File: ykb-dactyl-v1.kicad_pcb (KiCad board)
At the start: 2 copper layers, 1 part

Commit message: Update
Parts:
- removed U1: ~, holyiot-21069:holyiot-21069
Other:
- board outline added: 55.8 x 58.3 mm

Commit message: Update
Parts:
- added C1: C, Capacitor_SMD:C_0402_1005Metric, F.Cu at (128.1, 152.2)
- added C60: 0.1uF, Capacitor_SMD:C_0402_1005Metric, F.Cu at (130.9, 135.5)
- added C61: 0.1uF, Capacitor_SMD:C_0402_1005Metric, F.Cu at (130.9, 137.4)
- added IC1: TXU0101DCKR, footprints:SOT65P210X110-6N, F.Cu at (131.8, 132.6)
- added J1: JST_SH_BM10B-SRSS-TB_1x10-1MP_P1.00mm_Vertical, Connector_JST:JST_SH_BM10B-SRSS-TB_1x10-1MP_P1.00mm_Vertical, F.Cu at (90.0, 52.5)
- added J2: JST_SH_BM10B-SRSS-TB_1x10-1MP_P1.00mm_Vertical, Connector_JST:JST_SH_BM10B-SRSS-TB_1x10-1MP_P1.00mm_Vertical, F.Cu at (90.0, 58.0)
- added J3: JST_SH_BM10B-SRSS-TB_1x10-1MP_P1.00mm_Vertical, Connector_JST:JST_SH_BM10B-SRSS-TB_1x10-1MP_P1.00mm_Vertical, F.Cu at (90.0, 63.5)
- added J4: JST_SH_BM10B-SRSS-TB_1x10-1MP_P1.00mm_Vertical, Connector_JST:JST_SH_BM10B-SRSS-TB_1x10-1MP_P1.00mm_Vertical, F.Cu at (90.0, 69.0)
- added J5: JST_SH_BM10B-SRSS-TB_1x10-1MP_P1.00mm_Vertical, Connector_JST:JST_SH_BM10B-SRSS-TB_1x10-1MP_P1.00mm_Vertical, F.Cu at (87.8, 149.4)
- added J6: JST_SH_BM10B-SRSS-TB_1x10-1MP_P1.00mm_Vertical, Connector_JST:JST_SH_BM10B-SRSS-TB_1x10-1MP_P1.00mm_Vertical, F.Cu at (87.8, 155.6)
- added J7: JST_SH_BM12B-SRSS-TB_1x12-1MP_P1.00mm_Vertical, Connector_JST:JST_SH_BM12B-SRSS-TB_1x12-1MP_P1.00mm_Vertical, F.Cu at (103.6, 149.6)
- added J8: MC-121-L124, MC-121-L124:MC-121-L124, F.Cu at (90.1, 39.8)
- added J9: Conn_ARM_SWD_TagConnect_TC2030, Connector:Tag-Connect_TC2030-IDC-FP_2x03_P1.27mm_Vertical, F.Cu at (134.2, 126.0)
- added R1: 100K, Resistor_SMD:R_0402_1005Metric, F.Cu at (132.5, 152.0)
- added S1: DG9408EDN-T1-GE4, footprints:QFN65P400X400X95-17N-D, F.Cu at (98.4, 124.4)
- added S2: DG9408EDN-T1-GE4, footprints:QFN65P400X400X95-17N-D, F.Cu at (98.4, 130.7)
- added S3: DG9408EDN-T1-GE4, footprints:QFN65P400X400X95-17N-D, F.Cu at (98.4, 137.0)
- added S4: DG9408EDN-T1-GE4, footprints:QFN65P400X400X95-17N-D, F.Cu at (98.4, 143.3)
- added U1: holyiot-21069, holyiot-21069:holyiot-21069, F.Cu at (97.2, 78.2)
- added U2: XC6193A103ER-G, footprints:SON40P150X150X50-9N, F.Cu at (133.3, 149.4)
- added U3: TPS631000DRLR, footprints:SOT50P160X60-8N, F.Cu at (133.5, 145.6)
- added U4: TPS62840DLCR, footprints:SON50P200X150X100-8N, F.Cu at (129.2, 149.5)
- added U5: BQ25185DLHR, footprints:SON40P220X200X80-11N, F.Cu at (129.0, 145.9)
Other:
- outline, holes or cut-outs redrawn

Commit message: Update
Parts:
- added C21: 0.1uF, Capacitor_SMD:C_0402_1005Metric, F.Cu at (146.7, 103.1)
- added C22: 0.1uF, Capacitor_SMD:C_0402_1005Metric, F.Cu at (146.7, 105.1)
- added C31: 22uF, Capacitor_SMD:C_0402_1005Metric, F.Cu at (146.7, 107.1)
- added C32: 22uF, Capacitor_SMD:C_0402_1005Metric, F.Cu at (146.7, 109.0)
- added C33: 22uF, Capacitor_SMD:C_0402_1005Metric, F.Cu at (146.7, 111.0)
- added C41: 4.7uF, Capacitor_SMD:C_0402_1005Metric, F.Cu at (149.5, 103.1)
- added C42: 10uF, Capacitor_SMD:C_0402_1005Metric, F.Cu at (149.5, 105.1)
- added C51: 10uF, Capacitor_SMD:C_0402_1005Metric, F.Cu at (149.5, 107.1)
- added C52: 1uF, Capacitor_SMD:C_0402_1005Metric, F.Cu at (149.5, 109.0)
- added C53: 1uF, Capacitor_SMD:C_0402_1005Metric, F.Cu at (149.5, 111.0)
- added L31: 1uH, Inductor_SMD:L_0402_1005Metric, F.Cu at (137.9, 103.1)
- added L41: 2.2uH, Inductor_SMD:L_0402_1005Metric, F.Cu at (137.9, 105.1)
- added R101: 5.1K, Resistor_SMD:R_0402_1005Metric, F.Cu at (128.0, 62.0)
- added R102: 5.1K, Resistor_SMD:R_0402_1005Metric, F.Cu at (128.0, 64.0)
- added R31: 100K, Resistor_SMD:R_0402_1005Metric, F.Cu at (137.9, 107.1)
- added R32: 100K, Resistor_SMD:R_0402_1005Metric, F.Cu at (137.9, 109.1)
- added R33: 100K, Resistor_SMD:R_0402_1005Metric, F.Cu at (137.9, 111.1)
- added R34: 806K, Resistor_SMD:R_0402_1005Metric, F.Cu at (140.8, 103.1)
- added R35: 91K, Resistor_SMD:R_0402_1005Metric, F.Cu at (140.8, 105.1)
- added R41: 100K, Resistor_SMD:R_0402_1005Metric, F.Cu at (140.8, 107.1)
- added R42: 100K, Resistor_SMD:R_0402_1005Metric, F.Cu at (140.8, 109.1)
- added R43: 27K, Resistor_SMD:R_0402_1005Metric, F.Cu at (140.8, 111.1)
- added R44: 240K, Resistor_SMD:R_0402_1005Metric, F.Cu at (143.8, 103.1)
- added R51: 1K, Resistor_SMD:R_0402_1005Metric, F.Cu at (143.8, 105.1)
- added R52: 5K, Resistor_SMD:R_0402_1005Metric, F.Cu at (143.8, 107.1)
- added R53: 10K, Resistor_SMD:R_0402_1005Metric, F.Cu at (143.8, 109.1)
- added U6: USBLC6-2SC6, Package_TO_SOT_SMD:SOT-23-6, F.Cu at (124.0, 63.4)
- J9: value Conn_ARM_SWD_TagConnect_TC2030 -> Conn_ARM_SWD_TagConnect_TC2030_NL; footprint Connector:Tag-Connect_TC2030-IDC-FP_2x03_P1.27mm_Vertical -> Connector:Tag-Connect_TC2030-IDC-NL_2x03_P1.27mm_Vertical; moved to B.Cu
- moved J6 85.6 mm to (94.8, 70.3), turned to 90 degrees
- moved J7 79.6 mm to (101.7, 70.0), turned to 90 degrees
- moved J5 79.1 mm to (86.7, 70.3), turned to 90 degrees
- moved J9 78.9 mm to (56.6, 111.8), turned to 90 degrees
- moved U5 68.3 mm to (108.4, 80.8)
- moved S4 62.7 mm to (78.5, 83.8)
- moved R1 62.1 mm to (109.7, 94.2)
- moved U3 62.1 mm to (110.7, 87.8)
- moved C1 62.1 mm to (105.4, 94.4)
- moved U2 62.1 mm to (110.6, 91.5)
- moved U4 62.1 mm to (106.4, 91.7)
- moved IC1 54.5 mm to (104.5, 85.5)
- moved S1 53.3 mm to (72.5, 77.8)
- moved S2 53.2 mm to (72.3, 84.3)
- moved S3 53.1 mm to (72.2, 90.8)
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- renumbered C60 to C62
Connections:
- net /MCU/USB_DM_P renamed /MCU/USB_DN_P
- C61 pad 1: +3.3V -> +3.3V_SYS
- C62 pad 1: +5V -> +5V_SYS
- IC1 pad 1: +3.3V -> +3.3V_SYS
- IC1 pad 5: +5V -> +5V_SYS
- IC1 pad 6: +5V -> +5V_SYS
- J1 pad 8: +5V -> +5V_SYS
- J1 pad 9: +3.3V -> +3.3V_SYS
- J2 pad 8: +5V -> +5V_SYS
- J2 pad 9: +3.3V -> +3.3V_SYS
- J3 pad 8: +5V -> +5V_SYS
- J3 pad 9: +3.3V -> +3.3V_SYS
- J4 pad 8: +5V -> +5V_SYS
- J4 pad 9: +3.3V -> +3.3V_SYS
- J5 pad 8: +5V -> +5V_SYS
- J5 pad 9: +3.3V -> +3.3V_SYS
- J6 pad 8: +5V -> +5V_SYS
- J6 pad 9: +3.3V -> +3.3V_SYS
- J7 pad 10: +3.3V -> +3.3V_SYS
- J7 pad 9: +5V -> +5V_SYS
- J8 pad A1B12: unconnected-(J8-GND1-PadA1B12) -> GND
- J8 pad A4B9: unconnected-(J8-VBUS1-PadA4B9) -> +5V_USB
- J8 pad A5: unconnected-(J8-CC1-PadA5) -> Net-(J8-CC1)
- J8 pad A6: unconnected-(J8-DP1-PadA6) -> /USB/USB_DP
- J8 pad A7: unconnected-(J8-DN1-PadA7) -> /USB/USB_DN
- J8 pad B1A12: unconnected-(J8-GND2-PadB1A12) -> GND
- J8 pad B4A9: unconnected-(J8-VBUS2-PadB4A9) -> +5V_USB
- J8 pad B5: unconnected-(J8-CC2-PadB5) -> Net-(J8-CC2)
- J8 pad B6: unconnected-(J8-DP2-PadB6) -> /USB/USB_DP
- J8 pad B7: unconnected-(J8-DN2-PadB7) -> /USB/USB_DN
- J8 pad SHIELD: (no net) -> GND
- J9 pad 1: +3.3V -> +3.3V_SYS
- S1 pad 6: +3.3V -> +3.3V_SYS
- S2 pad 6: +3.3V -> +3.3V_SYS
- S3 pad 6: +3.3V -> +3.3V_SYS
- S4 pad 6: +3.3V -> +3.3V_SYS
- U1 pad VBUS: +5V -> +5V_SYS
- U1 pad VDD: +3.3V -> +3.3V_SYS
- U1 pad VDDH: +3.3V -> +3.3V_SYS
- U2 pad 1: unconnected-(U2-VIN-Pad1) -> VCC_PRESYS
- U2 pad 2: unconnected-(U2-NC-Pad2) -> GND
- U2 pad 5: unconnected-(U2-VSS-Pad5) -> GND
- U2 pad 6: unconnected-(U2-TEST-Pad6) -> GND
- U2 pad 7: unconnected-(U2-SHDN-Pad7) -> /Power/SHDN
- U2 pad 8: unconnected-(U2-VOUT-Pad8) -> VCC_SYS
- U2 pad 9: unconnected-(U2-EP-Pad9) -> GND
- U3 pad 1: unconnected-(U3-VOUT-Pad1) -> +5V_SYS
- U3 pad 2: unconnected-(U3-LX2-Pad2) -> Net-(U3-LX2)
- U3 pad 3: unconnected-(U3-LX1-Pad3) -> Net-(U3-LX1)
- U3 pad 4: unconnected-(U3-VIN-Pad4) -> VCC_SYS
- U3 pad 5: unconnected-(U3-EN-Pad5) -> Net-(U3-EN)
- U3 pad 6: unconnected-(U3-MODE-Pad6) -> Net-(U3-MODE)
- U3 pad 7: unconnected-(U3-GND-Pad7) -> GND
- U3 pad 8: unconnected-(U3-FB-Pad8) -> Net-(U3-FB)
- U4 pad 1: unconnected-(U4-GND-Pad1) -> GND
- U4 pad 2: unconnected-(U4-VIN-Pad2) -> +5V_SYS
- U4 pad 3: unconnected-(U4-MODE-Pad3) -> Net-(U4-MODE)
- U4 pad 4: unconnected-(U4-EN-Pad4) -> +5V_SYS
- U4 pad 5: unconnected-(U4-VSET-Pad5) -> Net-(U4-VSET)
- U4 pad 6: unconnected-(U4-STOP-Pad6) -> GND
- U4 pad 7: unconnected-(U4-SW-Pad7) -> Net-(U4-SW)
- U4 pad 8: unconnected-(U4-VOS-Pad8) -> +3.3V_SYS
- U5 pad 1: unconnected-(U5-SYS-Pad1) -> VCC_PRESYS
- U5 pad 10: unconnected-(U5-IN-Pad10) -> +5V_USB
- U5 pad 11: unconnected-(U5-EP-Pad11) -> GND
- U5 pad 2: unconnected-(U5-BAT-Pad2) -> +BATT
- U5 pad 3: unconnected-(U5-STAT2-Pad3) -> /Power/BAT_STAT_2
- U5 pad 4: unconnected-(U5-~{CE}-Pad4) -> GND
- U5 pad 5: unconnected-(U5-GND-Pad5) -> GND
- U5 pad 6: unconnected-(U5-TS/MR-Pad6) -> Net-(U5-TS/MR)
- U5 pad 7: unconnected-(U5-ILIM/VSET-Pad7) -> Net-(U5-ILIM/VSET)
- U5 pad 8: unconnected-(U5-ISET-Pad8) -> Net-(U5-ISET)
- U5 pad 9: unconnected-(U5-STAT1-Pad9) -> /Power/BAT_STAT_1

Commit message: Update
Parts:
- added C23: 0.1uF, Capacitor_SMD:C_0402_1005Metric, F.Cu at (37.8, 54.1)
- added D1: QLS6B-FKW, LED_SMD:LED_Cree-PLCC6_4.7x1.5mm, F.Cu at (39.5, 60.7)
- added R1: 1K, Resistor_SMD:R_0402_1005Metric, F.Cu at (34.9, 60.1)
- added R2: 1K, Resistor_SMD:R_0402_1005Metric, F.Cu at (34.9, 62.1)
- added R21: 5K, Resistor_SMD:R_0402_1005Metric, F.Cu at (34.9, 54.2)
- added R22: 200K, Resistor_SMD:R_0402_1005Metric, F.Cu at (34.9, 56.1)
- added R3: 1K, Resistor_SMD:R_0402_1005Metric, F.Cu at (34.9, 64.1)
- added S5: SKRTLAE010, footprints:SKRTLAE010, F.Cu at (37.6, 49.9)
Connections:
- U1 pad P0.14: unconnected-(U1-PadP0.14) -> /MCU/SHDN
- U1 pad P0.15: unconnected-(U1-PadP0.15) -> /MCU/DBG_LED
- U1 pad P0.17: unconnected-(U1-PadP0.17) -> /MCU/BAT_STAT_1
- U1 pad P0.18: unconnected-(U1-PadP0.18) -> /MCU/BAT_STAT_2
- U2 pad 3: unconnected-(U2-SW-Pad3) -> /Power/SW

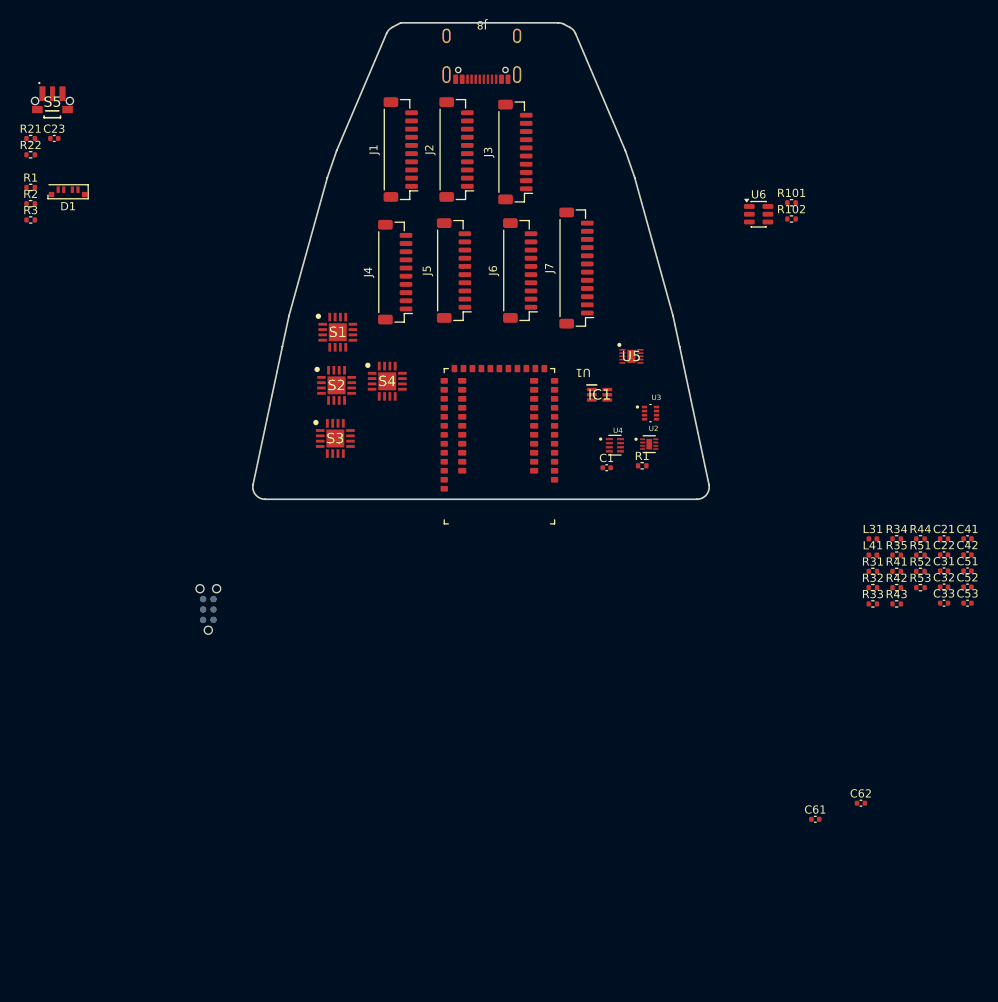
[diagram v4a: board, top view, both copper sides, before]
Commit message: Modify placment of component
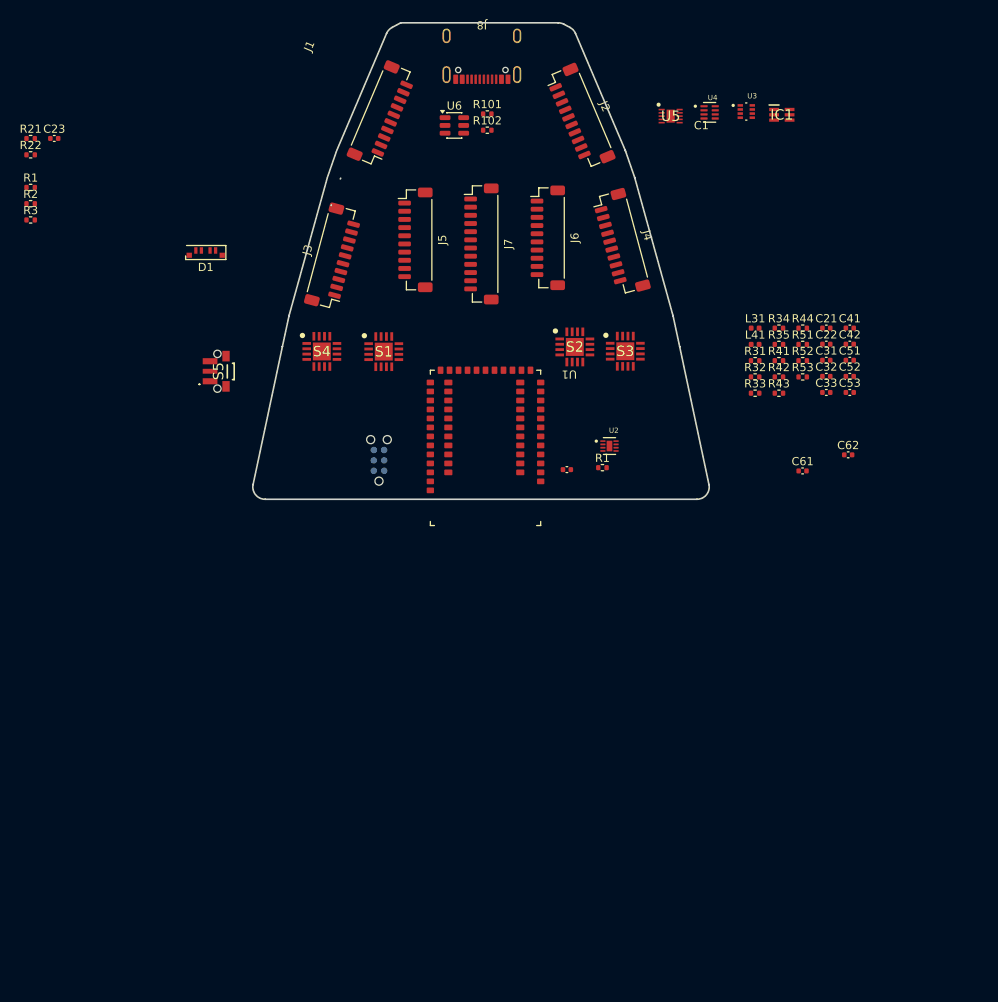
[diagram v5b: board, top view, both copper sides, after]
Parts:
- moved C61 42.6 mm to (129.3, 94.8)
- moved C62 42.6 mm to (134.9, 92.8)
- moved U4 42.3 mm to (118.0, 51.0)
- moved IC1 40.9 mm to (126.8, 51.2)
- moved R102 38.8 mm to (90.8, 53.1)
- moved U6 38.8 mm to (86.7, 52.5)
- moved R101 38.8 mm to (90.8, 51.1)
- moved U3 38.7 mm to (122.5, 50.9)
- moved S5 38.6 mm to (58.1, 82.6), turned to 90 degrees
- moved S3 37.0 mm to (107.7, 80.2)
- moved U5 29.8 mm to (113.2, 51.4)
- moved C21 29.5 mm to (132.2, 77.3)
- moved C22 29.5 mm to (132.2, 79.3)
- moved C31 29.5 mm to (132.2, 81.3)
- moved C32 29.5 mm to (132.2, 83.2)
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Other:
- outline, holes or cut-outs redrawn
